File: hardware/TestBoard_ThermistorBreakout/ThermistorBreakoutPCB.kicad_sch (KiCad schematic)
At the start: 6 parts, among them J1 Conn_01x02, J8 Conn_01x06

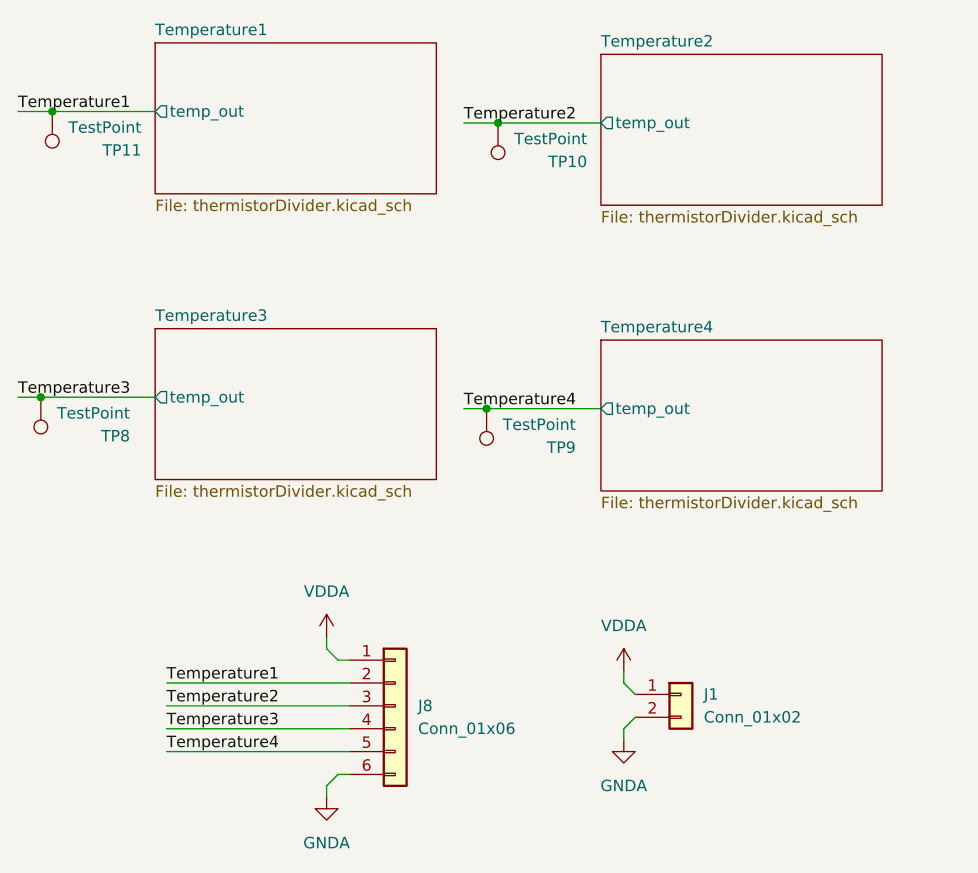
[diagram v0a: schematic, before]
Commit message: Temperature Scrutineering PCB (#22)
* initial schematic and layout

* updated layout

* schematic with graphics/mounting

* graphics stuff

* fixed routing

* BOM and gerber (still need to find jack P/N)

* final

* revert back to main...

* added Scrutineering footprints

* added Scrutineering 3d models

* BOM and gerber with changed connector

* changed to vertical connectors

* added footprints/3d models vertical connectors

* fix 1 trace

* updated BOM

* updated BOM again

* Revert "fix 1 trace"

This reverts commit af0c854c5f9be3b18890f8714f235c97d2fe5d90.

:#

* Replaced Lakshay's tiny banana jacks with real ones

* fix unrouted

* Updated Gerbers

* Updated Thermistor Test Board

---------

Co-authored-by: Phoenix Nguyen <phoenixn831@gmail.com>
Co-authored-by: Ravi Shah <ravidhruvishshah@gmail.com>
Co-authored-by: kretsdyl <kretschmandk@gmail.com>
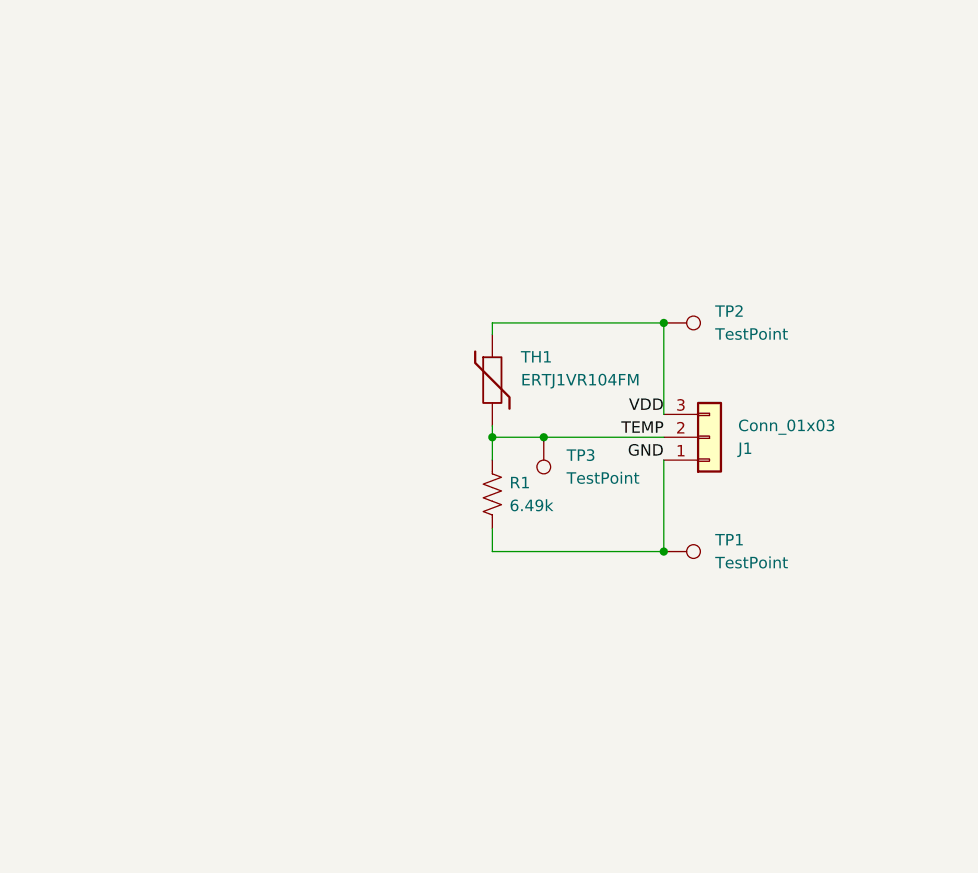
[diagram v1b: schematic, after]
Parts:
- removed J1: Conn_01x02, Connector_PinHeader_2.54mm:PinHeader_1x02_P2.54mm_Vertical, symbol Connector_Generic:Conn_01x02
- removed J8: Conn_01x06, VoltTemp:1053131106, symbol Connector_Generic:Conn_01x06
- removed TP10, TP11, TP8, TP9: TestPoint, TestPoint:TestPoint_Keystone_5005-5009_Compact, symbol Connector:TestPoint
- added J1: Conn_01x03, Scrutineering:CONN_SD-105309-100_03_MOL, symbol Connector_Generic:Conn_01x03
- added R1: 6.49k, Resistor_SMD:R_0603_1608Metric_Pad0.98x0.95mm_HandSolder, symbol Device:R_US
- added TH1: ERTJ1VR104FM, Resistor_SMD:R_0603_1608Metric_Pad0.98x0.95mm_HandSolder, symbol Device:Thermistor
- added TP1, TP2, TP3: TestPoint, TestPoint:TestPoint_Pad_2.0x2.0mm, symbol Connector:TestPoint
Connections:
- new net GND: J1.1 (Pin_1), R1.2, TP1.1
- new net TEMP: J1.2 (Pin_2), R1.1, TH1.2, TP3.1
- new net VDD: J1.3 (Pin_3), TH1.1, TP2.1
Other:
- removed sheet Temperature1
- removed sheet Temperature2
- removed sheet Temperature3
- removed sheet Temperature4
